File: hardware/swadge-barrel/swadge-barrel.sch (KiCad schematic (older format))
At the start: 46 parts, among them J1 USB_B_Micro, Q1 Q_NPN_BEC, SW1 SW_SPDT, U1 ESP-13-WROOM-02D, U2 OLED_DISPLAY, U3 BUS_PCIexpress, U4 QMA6981, U5 AP1117-33, U6 OLED_CONNECTOR

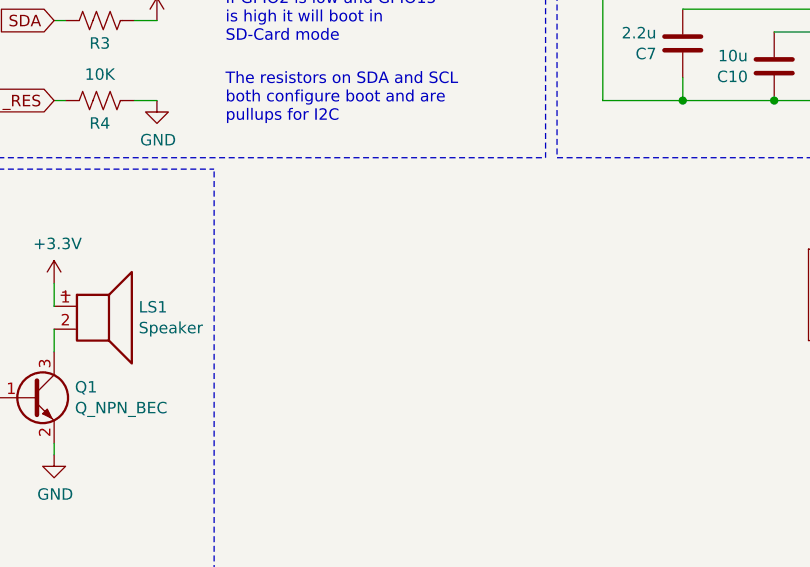
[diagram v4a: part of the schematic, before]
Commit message: Added headband part and 3D model
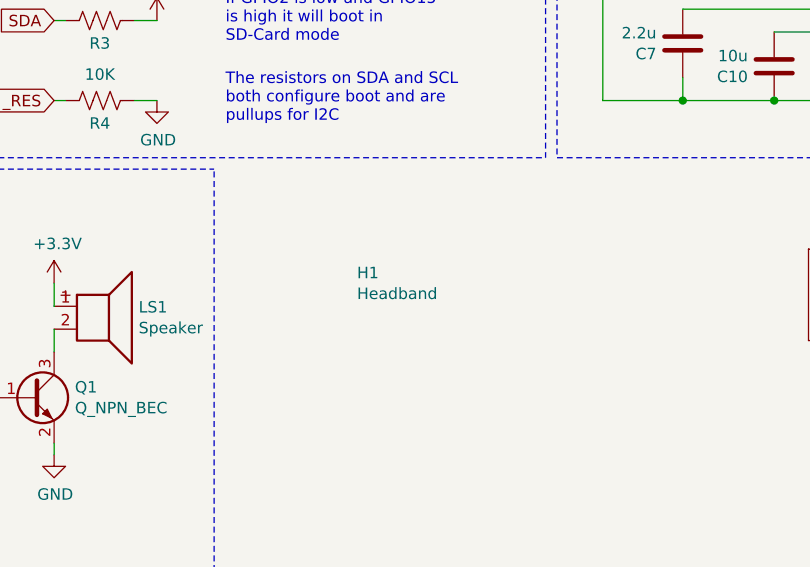
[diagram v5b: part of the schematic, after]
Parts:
- added H1: Headband, Swadge_Parts:Headband, symbol Swadge_Parts:Headband
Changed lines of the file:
@@
+	1    0    0    -1
+$EndComp
+$Comp
+L Swadge_Parts:Headband H1
+U 1 1 5D829692
+P 2800 6450
+F 0 "H1" H 2825 6496 50  0000 L CNN
+F 1 "Headband" H 2825 6405 50  0000 L CNN
+F 2 "Swadge_Parts:Headband" H 2800 6450 50  0001 C CNN
+F 3 "" H 2800 6450 50  0001 C CNN
+	1    2800 6450
 	1    0    0    -1
 $EndComp

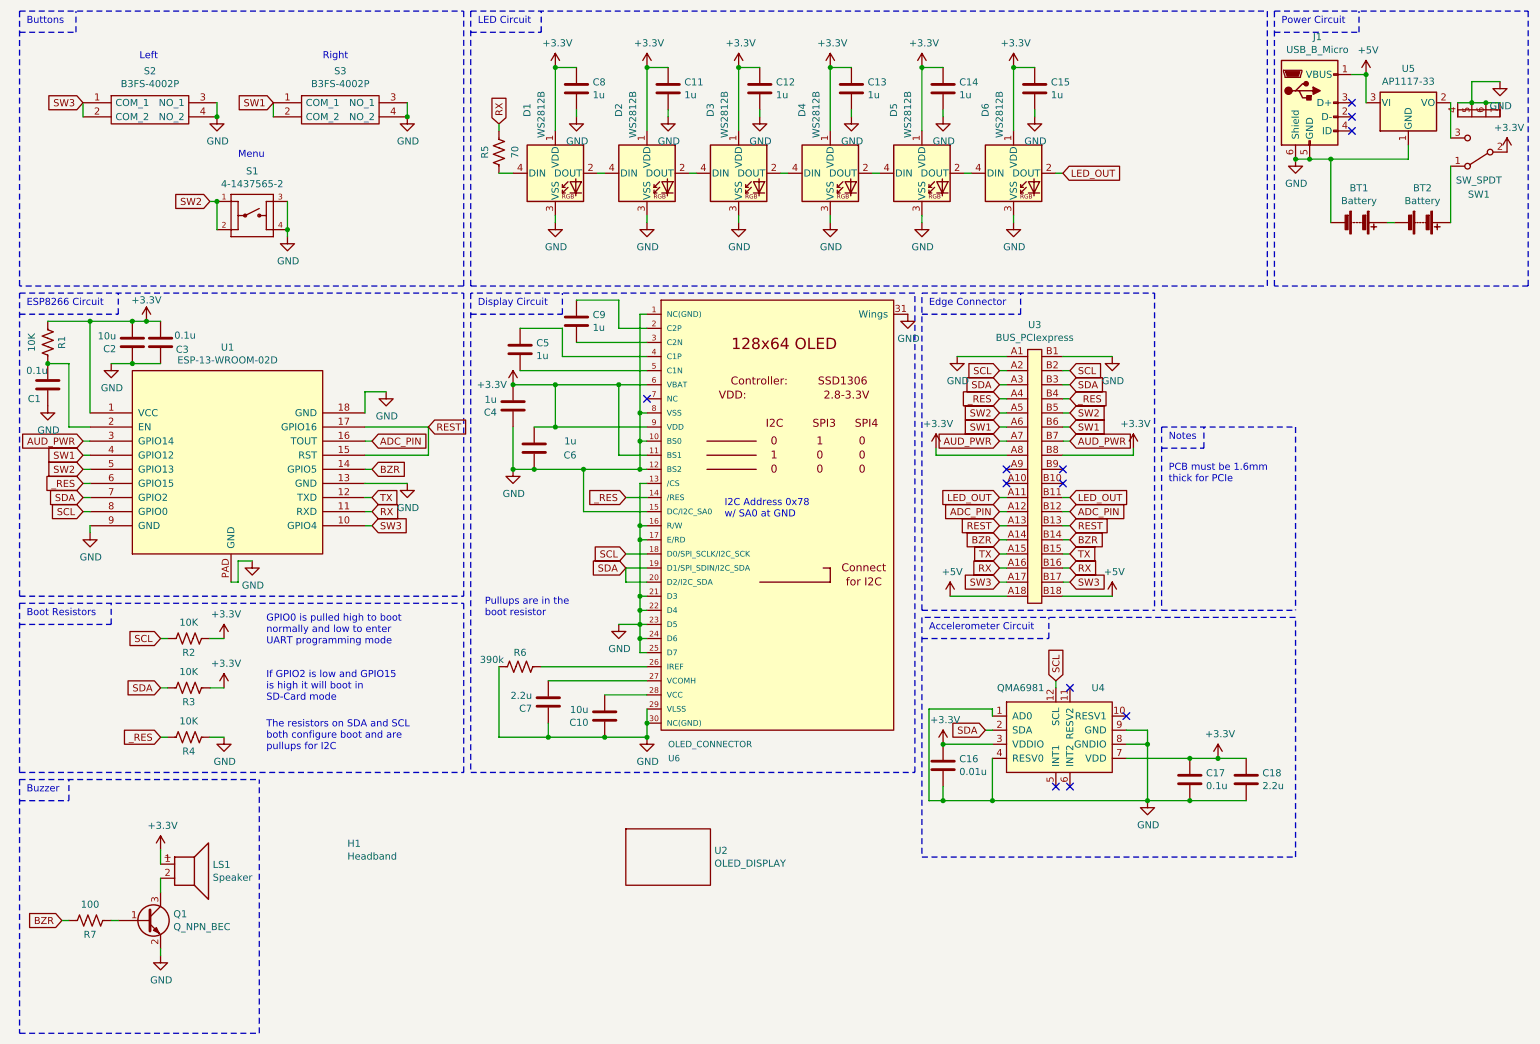
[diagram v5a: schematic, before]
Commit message: Removed transistor from the buzzer circuit. It's louder this way Updated buzzer part info Updated headband part info Adjusted orientation of accelerometer passives
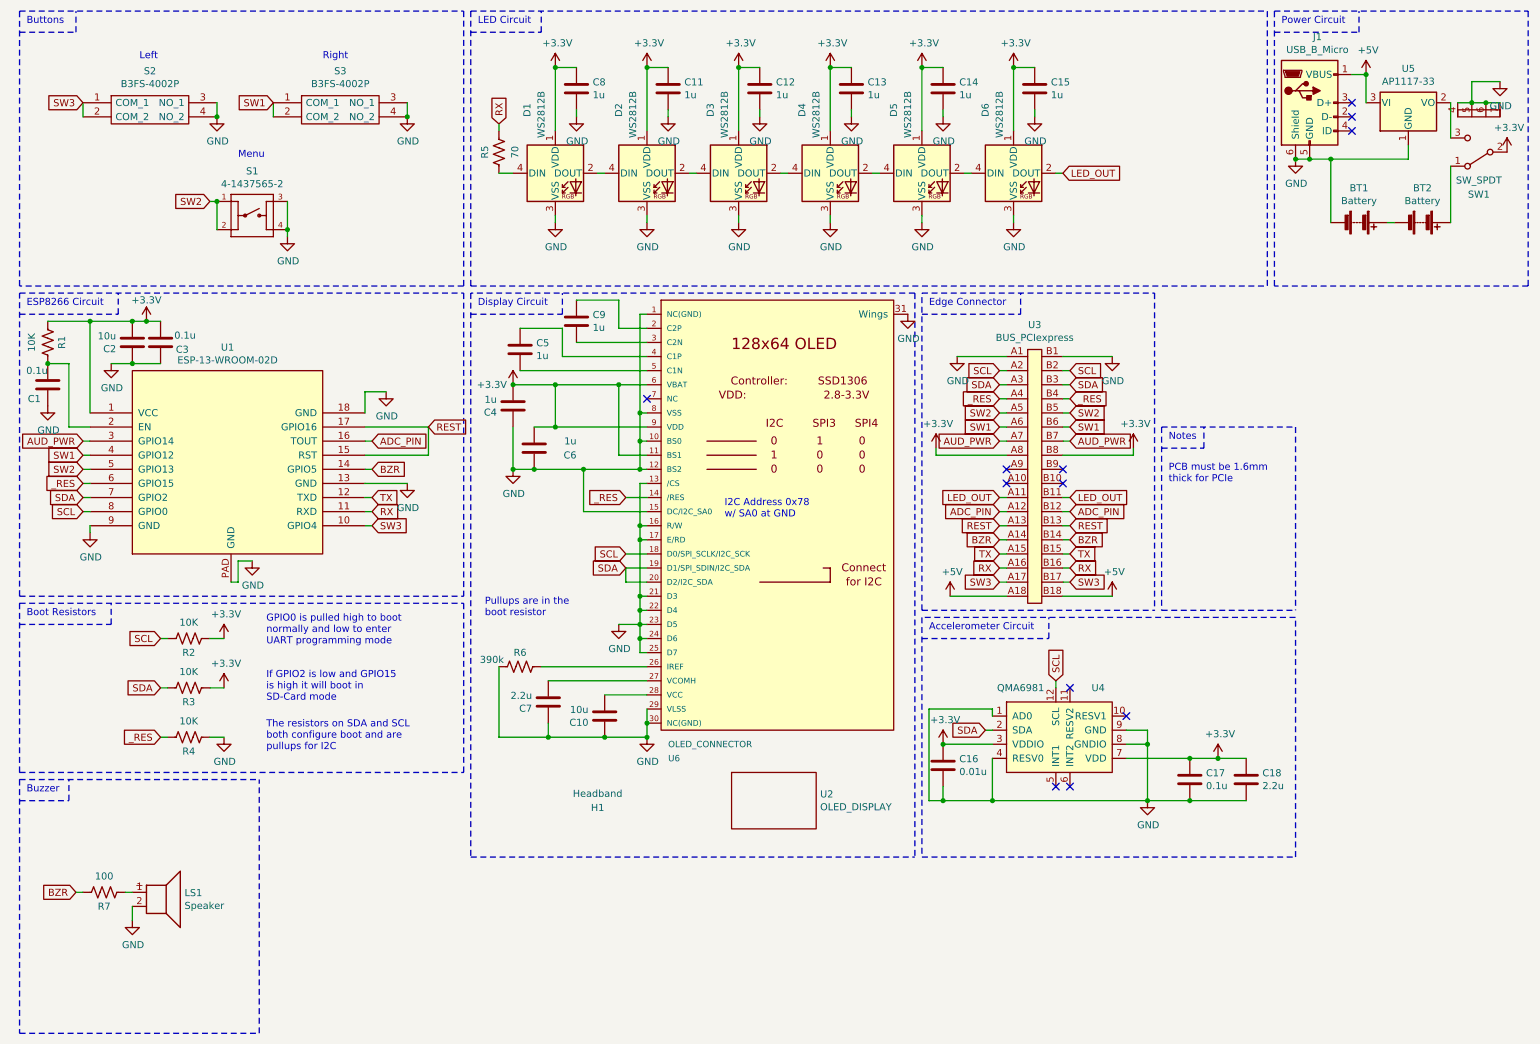
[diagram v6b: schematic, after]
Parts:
- removed Q1: Q_NPN_BEC, Swadge_Parts:SOT-23, symbol Swadge_Parts:Q_NPN_BEC
- H1: Digikey (none) -> 952-3598-ND; Notes (none) -> Use Swadge Headband PCB and two 2x1 male pin headers with 1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; Substitutable (none) -> N
- LS1: Cost100 13.48 -> 9.32; Digikey LCSC Part #C96102 -> LCSC Part #C219727; Notes Use magnetic buzzer. 3V rated. 9mm diameter. 5mm between th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 -> Use piezo buzzer. 1 ~ 25V operating voltage. 12.5mm diamete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
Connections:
- net +3V3: no longer LS1.1
- net GND: now also LS1.2
- net at R7.1: now also LS1.1
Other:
- moved on the sheet: LS1, R7, U2
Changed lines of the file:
@@
 	6850 2500 3700 2500
 Wire Notes Line
-	3700 2500 3700 5900
-Wire Notes Line
-	3700 5900 6850 5900
-Wire Notes Line
-	6850 5900 6850 2500
+	3700 6500 6850 6500
 Text Notes 3750 2600 0    50   ~ 0
 Display Circuit
@@
 Wire Notes Line
 	3650 500  3650 2450
-$Comp
-L Swadge_Parts:Q_NPN_BEC Q1
-U 1 1 5D5EC406
-P 1400 6950
-F 0 "Q1" H 1591 6996 50  0000 L CNN
-F 1 "Q_NPN_BEC" H 1591 6905 50  0000 L CNN
-F 2 "Swadge_Parts:SOT-23" H 2050 7300 50  0001 C CNN
-F 3 "https://www.onsemi.com/pub/Collateral/BC846ALT1-D.PDF" H 1400 6950 50  0001 C CNN
-F 4 "BC848BLT3GOSTR-ND" H 2050 7200 50  0001 C CNN "Digikey"
-F 5 "1.554" H 1750 7400 50  0001 C CNN "Cost100"
-F 6 "Y" H 1700 7500 50  0001 C CNN "Substitutable"
-F 7 "Use any NPN transistor in SOT-23 package with the same leads as BC848BLT3G (1=base. 2=emitter. 3=collector)" H 1400 6950 50  0001 C CNN "Notes"
-	1    1400 6950
-	1    0    0    -1
-$EndComp
-$Comp
-L power:+3.3V #PWR033
-U 1 1 5D5EE737
-P 1500 6450
-F 0 "#PWR033" H 1500 6300 50  0001 C CNN
-F 1 "+3.3V" H 1515 6623 50  0000 C CNN
-F 2 "" H 1500 6450 50  0001 C CNN
-F 3 "" H 1500 6450 50  0001 C CNN
-	1    1500 6450
-	1    0    0    -1
-$EndComp
-Text GLabel 800  6950 0    50   Input ~ 0
+Text GLabel 900  6750 0    50   Input ~ 0
 BZR
 Wire Wire Line
-	1150 6950 1200 6950
+	1250 6750 1300 6750
 $Comp
 L power:GND #PWR048
 U 1 1 5D5FD0B6
-P 1500 7200
-F 0 "#PWR048" H 1500 6950 50  0001 C CNN
-F 1 "GND" H 1505 7027 50  0000 C CNN
-F 2 "" H 1500 7200 50  0001 C CNN
-F 3 "" H 1500 7200 50  0001 C CNN
-	1    1500 7200
-	1    0    0    -1
-$EndComp
-Wire Wire Line
-	1500 7150 1500 7200
+P 1300 6950
+F 0 "#PWR048" H 1300 6700 50  0001 C CNN
+F 1 "GND" H 1305 6777 50  0000 C CNN
+F 2 "" H 1300 6950 50  0001 C CNN
+F 3 "" H 1300 6950 50  0001 C CNN
+	1    1300 6950
+	1    0    0    -1
+$EndComp
 $Comp
 L Swadge_Parts:R_US R7
 U 1 1 5D60B5AD
-P 1000 6950
-F 0 "R7" V 1100 6950 50  0000 C CNN
-F 1 "100" V 886 6950 50  0000 C CNN
-F 2 "Swadge_Parts:R_0603_1608Metric" V 1040 6940 50  0001 C CNN
-F 3 "" H 1000 6950 50  0001 C CNN
-F 4 "10" H -700 1300 50  0001 C CNN "Cost100"
-F 5 "RNCP0603FTD10K0CT-ND" H -700 1300 50  0001 C CNN "Digikey"
-F 6 "Y" H -700 1300 50  0001 C CNN "Substitutable"
-F 7 "0603 Package" H 1000 6950 50  0001 C CNN "Notes"
-	1    1000 6950
+P 1100 6750
+F 0 "R7" V 1200 6750 50  0000 C CNN
+F 1 "100" V 986 6750 50  0000 C CNN
+F 2 "Swadge_Parts:R_0603_1608Metric" V 1140 6740 50  0001 C CNN
+F 3 "" H 1100 6750 50  0001 C CNN
+F 4 "10" H -600 1100 50  0001 C CNN "Cost100"
+F 5 "RNCP0603FTD10K0CT-ND" H -600 1100 50  0001 C CNN "Digikey"
+F 6 "Y" H -600 1100 50  0001 C CNN "Substitutable"
+F 7 "0603 Package" H 1100 6750 50  0001 C CNN "Notes"
+	1    1100 6750
 	0    1    1    0
 $EndComp
 Wire Wire Line
-	800  6950 850  6950
+	900  6750 950  6750
 Wire Notes Line
 	500  5950 500  7750
@@
 L Swadge_Parts:Speaker LS1
 U 1 1 5D6E9B01
-P 1700 6550
-F 0 "LS1" H 1870 6546 50  0000 L CNN
-F 1 "Speaker" H 1870 6455 50  0000 L CNN
-F 2 "Swadge_Parts:Buzzer_12x9.5RM7.6" H 1700 6350 50  0001 C CNN
-F 3 "https://datasheet.lcsc.com/szlcsc/Jiangsu-Huaneng-Elec-HNB09A03_C96102.pdf" H 1690 6500 50  0001 C CNN
-F 4 "LCSC Part #C96102" H 1300 6900 50  0001 C CNN "Digikey"
-F 5 "13.48" H 1950 6800 50  0001 C CNN "Cost100"
-F 6 "Y" H 1950 7050 50  0001 C CNN "Substitutable"
-F 7 "Use magnetic buzzer. 3V rated. 9mm diameter. 5mm between the leads" H 1400 7000 50  0001 C CNN "Notes"
-	1    1700 6550
-	1    0    0    -1
-$EndComp
-Wire Wire Line
-	1500 6650 1500 6750
-Wire Wire Line
-	1500 6450 1500 6550
+P 1500 6750
+F 0 "LS1" H 1670 6746 50  0000 L CNN
+F 1 "Speaker" H 1670 6655 50  0000 L CNN
+F 2 "Swadge_Parts:Buzzer_12x9.5RM7.6" H 1500 6550 50  0001 C CNN
+F 3 "https://datasheet.lcsc.com/szlcsc/1808301434_ZLFY-ZL-YDW1207-4005PA-5-0_C219727.pdf" H 1490 6700 50  0001 C CNN
+F 4 "LCSC Part #C219727" H 1100 7100 50  0001 C CNN "Digikey"
+F 5 "9.32" H 1750 7000 50  0001 C CNN "Cost100"
+F 6 "Y" H 1750 7250 50  0001 C CNN "Substitutable"
+F 7 "Use piezo buzzer. 1 ~ 25V operating voltage. 12.5mm diameter. 5mm between the leads" H 1200 7200 50  0001 C CNN "Notes"
+	1    1500 6750
+	1    0    0    -1
+$EndComp
+Wire Wire Line
+	1300 6850 1300 6950
 Wire Notes Line
 	500  5950 2200 5950
@@
 L Swadge_Parts:OLED_DISPLAY U2
 U 1 1 5D78A9AC
-P 5100 6500
-F 0 "U2" H 5428 6546 50  0000 L CNN
-F 1 "OLED_DISPLAY" H 5428 6455 50  0000 L CNN
-F 2 "Swadge_Parts:NULL" H 5100 6500 50  0001 C CNN
-F 3 "https://www.buydisplay.com/download/ic/SSD1306.pdf" H 5100 6500 50  0001 C CNN
-F 4 "https://www.buydisplay.com/download/manual/ER-OLED0.96-1_Series_Datasheet.pdf" H 5100 6500 50  0001 C CNN "Datasheet2"
-F 5 "EastRising# ER-OLED0.96-1.3W" H 5100 6500 50  0001 C CNN "Digikey"
-F 6 "352" H 5100 6500 50  0001 C CNN "Cost100"
-F 7 "Y" H 5100 6500 50  0001 C CNN "Substitutable"
-F 8 "Must be a single color. white. Must have SSD1306 driver. Must have top pins. 0.5mm pitch. like the connector" H 5100 6500 50  0001 C CNN "Notes"
-	1    5100 6500
+P 5850 6100
+F 0 "U2" H 6178 6146 50  0000 L CNN
+F 1 "OLED_DISPLAY" H 6178 6055 50  0000 L CNN
+F 2 "Swadge_Parts:NULL" H 5850 6100 50  0001 C CNN
+F 3 "https://www.buydisplay.com/download/ic/SSD1306.pdf" H 5850 6100 50  0001 C CNN
+F 4 "https://www.buydisplay.com/download/manual/ER-OLED0.96-1_Series_Datasheet.pdf" H 5850 6100 50  0001 C CNN "Datasheet2"
+F 5 "EastRising# ER-OLED0.96-1.3W" H 5850 6100 50  0001 C CNN "Digikey"
+F 6 "352" H 5850 6100 50  0001 C CNN "Cost100"
+F 7 "Y" H 5850 6100 50  0001 C CNN "Substitutable"
+F 8 "Must be a single color. white. Must have SSD1306 driver. Must have top pins. 0.5mm pitch. like the connector" H 5850 6100 50  0001 C CNN "Notes"
+	1    5850 6100
 	1    0    0    -1
 $EndComp
@@
 L Swadge_Parts:Headband H1
 U 1 1 5D829692
-P 2800 6450
-F 0 "H1" H 2825 6496 50  0000 L CNN
-F 1 "Headband" H 2825 6405 50  0000 L CNN
-F 2 "Swadge_Parts:Headband" H 2800 6450 50  0001 C CNN
-F 3 "" H 2800 6450 50  0001 C CNN
-	1    2800 6450
-	1    0    0    -1
-$EndComp
+P 4600 6150
+F 0 "H1" H 4600 6150 50  0000 C CNN
+F 1 "Headband" H 4600 6250 50  0000 C CNN
+F 2 "Swadge_Parts:Headband" H 4600 6150 50  0001 C CNN
+F 3 "https://cdn.harwin.com/pdfs/M50-353.pdf" H 4600 6150 50  0001 C CNN
+F 4 "" H 4600 6150 50  0001 C CNN "Cost100"
+F 5 "952-3598-ND" H 4600 6150 50  0001 C CNN "Digikey"
+F 6 "Use Swadge Headband PCB and two 2x1 male pin headers with 1.27mm spacing for assembly. Must attach OLED display before soldering headband. This is meant to protect the OLED's corners" H 4600 6150 50  0001 C CNN "Notes"
+F 7 "N" H 4600 6150 50  0001 C CNN "Substitutable"
+	1    4600 6150
+	1    0    0    -1
+$EndComp
+Wire Notes Line
+	3700 2500 3700 6500
+Wire Notes Line
+	6850 2500 6850 6500
 $EndSCHEMATC

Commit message: Removed some capacitance from 3.3V, added some capacitance to 5V
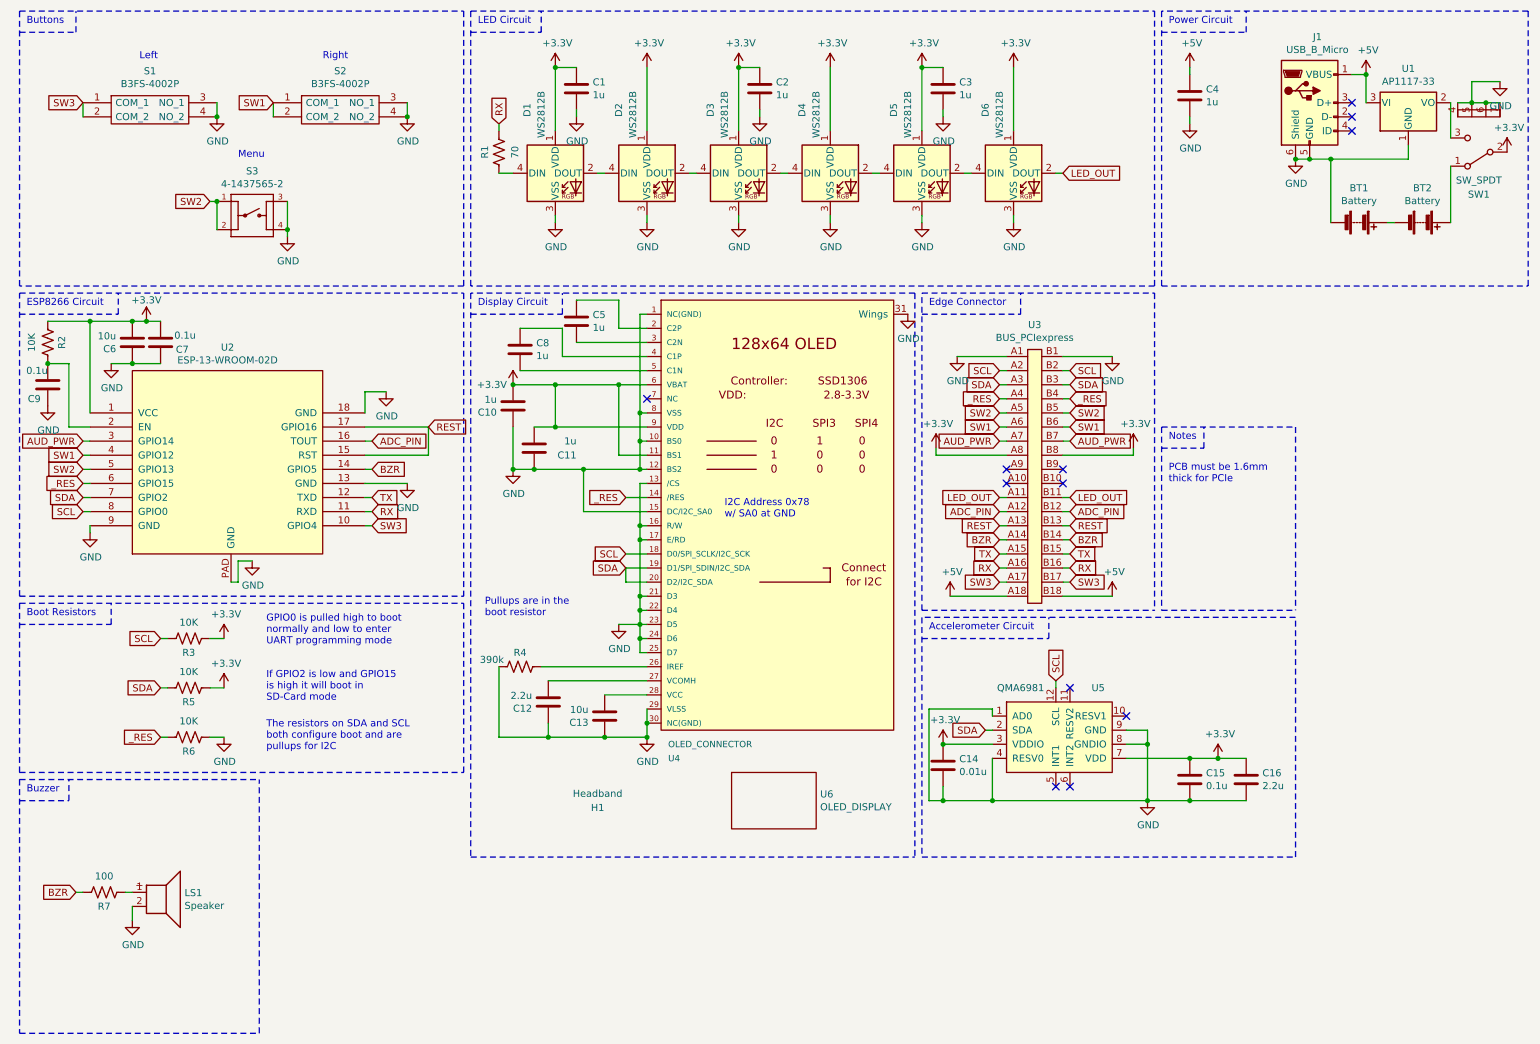
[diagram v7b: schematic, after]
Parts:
- removed C13, C15: 1u, Swadge_Parts:C_0603_1608Metric, symbol Swadge_Parts:C
- renumbered C8 to C1, C4 to C10, C6 to C11, C7 to C12, C10 to C13, C16 to C14, C17 to C15, C18 to C16, C12 to C2, C14 to C3, C11 to C4, C9 to C5, C2 to C6, C3 to C7, C5 to C8, C1 to C9, R5 to R1, R1 to R2, R2 to R3, R6 to R4, R3 to R5, R4 to R6, S2 to S1, S3 to S2, S1 to S3, U5 to U1, U1 to U2, U6 to U4, U4 to U5, U2 to U6
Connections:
- net +3V3: no longer C4.1
- net +5V: now also C4.1
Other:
- moved on the sheet: C4

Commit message: Updated BOM notes
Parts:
- U4: Digikey LCSC #C11095 -> LCSC Part #C11060; Notes Must have top contacts. same as the OLED -> Must have bottom contacts. same as the OLED
- U6: Digikey EastRising# ER-OLED0.96-1.3W -> EastRising# ER-OLED0.96-1.1W; Notes Must be a single color. white. Must have SSD1306 driver. Mu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 -> Must be a single color, white. Must have SSD1306 driver. Mu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
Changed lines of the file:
@@
 F 3 "https://datasheet.lcsc.com/szlcsc/JUSHUO-AFC07-S30ECC-00_C11095.pdf" H 5950 4050 50  0001 C CNN
 F 4 "119" H 0   0   50  0001 C CNN "Cost100"
-F 5 "LCSC #C11095" H 0   0   50  0001 C CNN "Digikey"
+F 5 "LCSC Part #C11060" H 0   0   50  0001 C CNN "Digikey"
 F 6 "Y" H 0   0   50  0001 C CNN "Substitutable"
-F 7 "Must have top contacts. same as the OLED" H 5950 4050 50  0001 C CNN "Notes"
+F 7 "Must have bottom contacts. same as the OLED" H 5950 4050 50  0001 C CNN "Notes"
 	1    5950 4050
 	1    0    0    -1
@@
 F 3 "https://www.buydisplay.com/download/ic/SSD1306.pdf" H 5850 6100 50  0001 C CNN
 F 4 "https://www.buydisplay.com/download/manual/ER-OLED0.96-1_Series_Datasheet.pdf" H 5850 6100 50  0001 C CNN "Datasheet2"
-F 5 "EastRising# ER-OLED0.96-1.3W" H 5850 6100 50  0001 C CNN "Digikey"
+F 5 "EastRising# ER-OLED0.96-1.1W" H 5850 6100 50  0001 C CNN "Digikey"
 F 6 "352" H 5850 6100 50  0001 C CNN "Cost100"
 F 7 "Y" H 5850 6100 50  0001 C CNN "Substitutable"
-F 8 "Must be a single color. white. Must have SSD1306 driver. Must have top pins. 0.5mm pitch. like the connector" H 5850 6100 50  0001 C CNN "Notes"
+F 8 "Must be a single color, white. Must have SSD1306 driver. Must have bottom pins, same as connector. 0.5mm pitch, like the connector" H 5850 6100 50  0001 C CNN "Notes"
 	1    5850 6100
 	1    0    0    -1
@@
 F 2 "Swadge_Parts:Headband" H 4600 6150 50  0001 C CNN
 F 3 "https://cdn.harwin.com/pdfs/M50-353.pdf" H 4600 6150 50  0001 C CNN
-F 4 "" H 4600 6150 50  0001 C CNN "Cost100"
-F 5 "952-3598-ND" H 4600 6150 50  0001 C CNN "Digikey"
-F 6 "Use Swadge Headband PCB and two 2x1 male pin headers with 1.27mm spacing for assembly. Must attach OLED display before soldering headband. This is meant to protect the OLED's corners" H 4600 6150 50  0001 C CNN "Notes"
-F 7 "N" H 4600 6150 50  0001 C CNN "Substitutable"
+F 4 "952-3598-ND" H 4600 6150 50  0001 C CNN "Digikey"
+F 5 "Use Swadge Headband PCB and two 2x1 male pin headers with 1.27mm spacing for assembly. Must attach OLED display before soldering headband. This is meant to protect the OLED's corners" H 4600 6150 50  0001 C CNN "Notes"
+F 6 "N" H 4600 6150 50  0001 C CNN "Substitutable"
 	1    4600 6150
 	1    0    0    -1
